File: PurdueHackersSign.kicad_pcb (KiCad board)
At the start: 2 copper layers, 73.7 x 134.6 mm, 43 parts, among them J1 Screw_Terminal_01x06, J2 Screw_Terminal_01x04, J3 Screw_Terminal_01x04, J4 Screw_Terminal_01x04, J5 Screw_Terminal_01x04, J6 Screw_Terminal_01x04, Q1 Q_NMOS_GDS, Q10 Q_NMOS_GDS, Q11 Q_NMOS_GDS, Q12 Q_NMOS_GDS, Q13 Q_NMOS_GDS, Q14 Q_NMOS_GDS, Q15 Q_NMOS_GDS, Q2 Q_NMOS_GDS, Q3 Q_NMOS_GDS, Q4 Q_NMOS_GDS, Q5 Q_NMOS_GDS, Q6 Q_NMOS_GDS, Q7 Q_NMOS_GDS, Q8 Q_NMOS_GDS, Q9 Q_NMOS_GDS, U1 RaspberryPi_Pico_W, U2 L7805, U3 25LCxxx

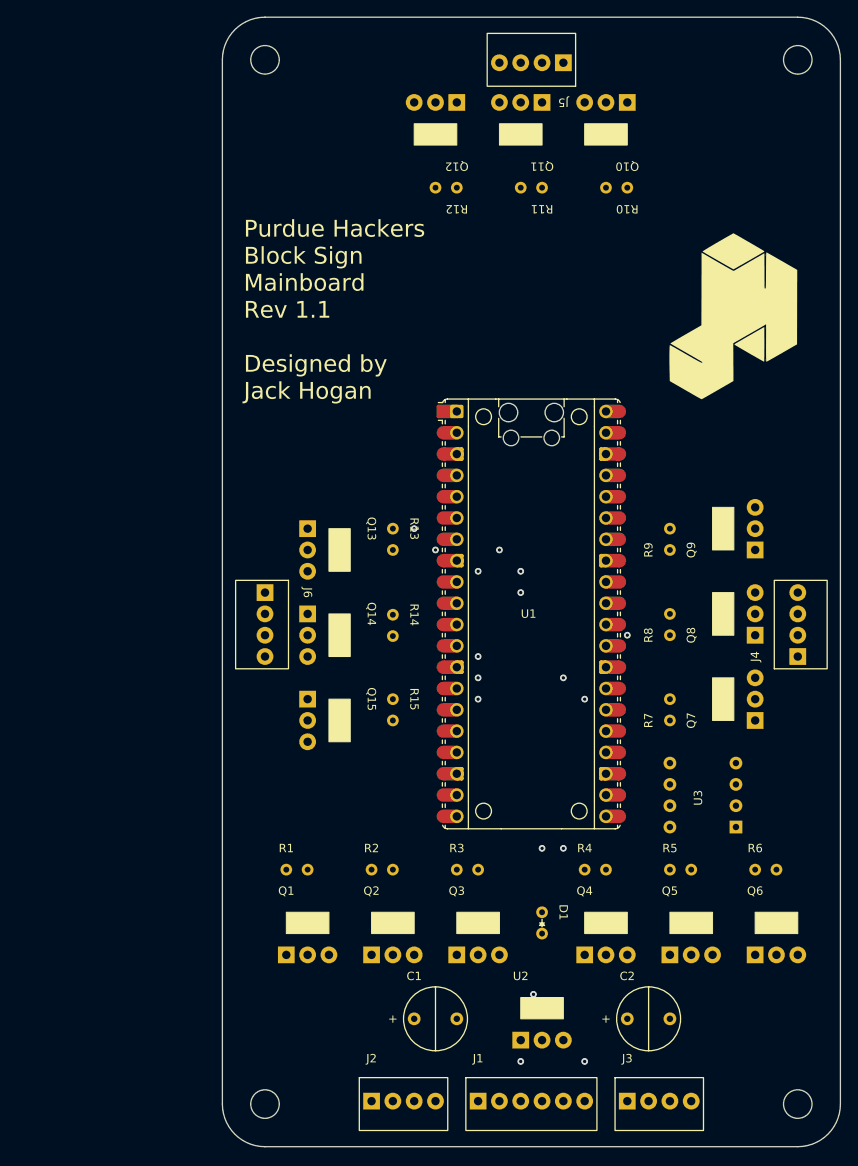
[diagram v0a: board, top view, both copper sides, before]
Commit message: Re-drew the schematic, re-assigned all the symbols, and re-routed the PCB
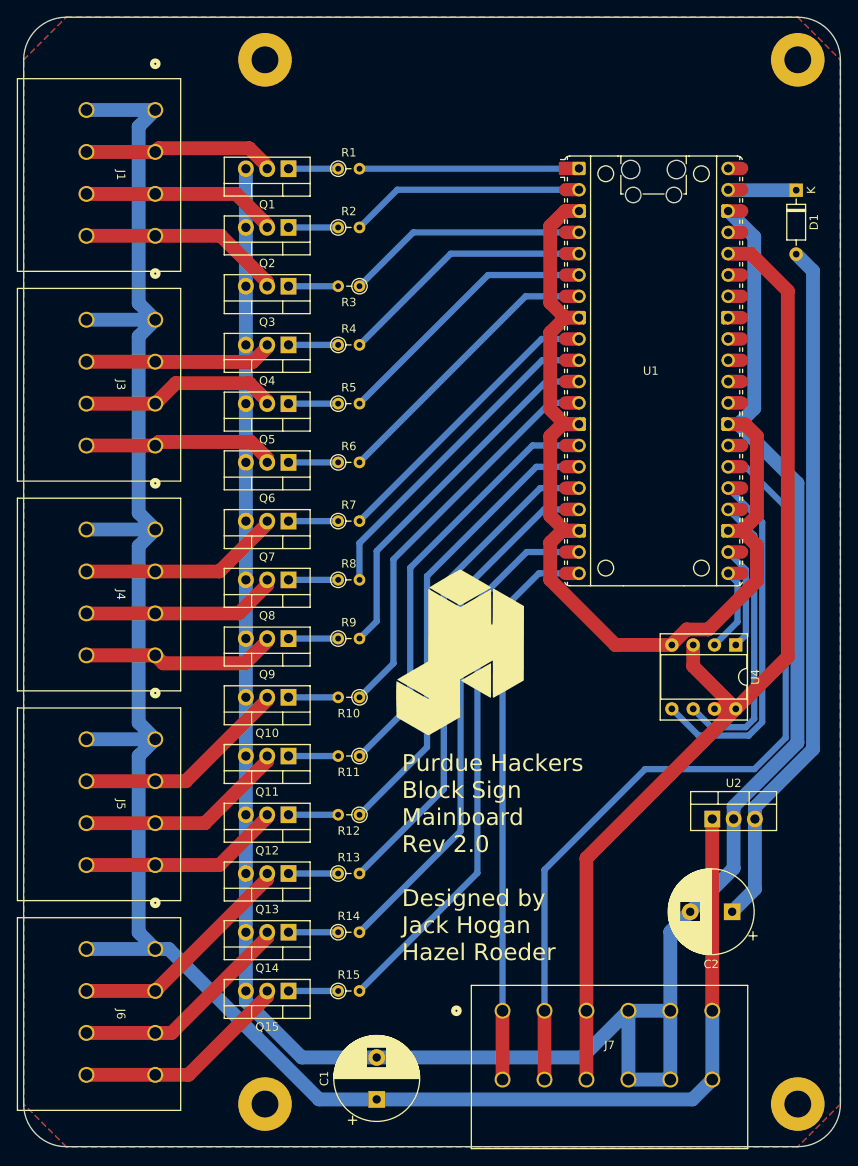
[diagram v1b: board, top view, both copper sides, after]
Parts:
- removed J2: Screw_Terminal_01x04, UsefulComponents:TerminalBlock_Adafruit-4
- removed U3: 25LCxxx, UsefulComponents:25LC1024
- added ?: , , F.Cu at (81.3, 33.0)
- added ?: , , F.Cu at (144.8, 157.5)
- added ?: , , F.Cu at (144.8, 33.0)
- added J7: 2604-1106, Local Footprints:CONN_2604-1106_WAG, F.Cu at (109.6, 146.4)
- added REF**: MountingHole_3.2mm_M3_Pad, MountingHole:MountingHole_3.2mm_M3_Pad, F.Cu at (81.3, 157.5)
- added U4: 25LCxxx, Package_DIP:DIP-8_W7.62mm_Socket, F.Cu at (137.4, 102.8)
- C1, C2: footprint UsefulComponents:PolarizedCapacitor -> Capacitor_THT:CP_Radial_D10.0mm_P5.00mm
- D1: footprint UsefulComponents:Diode -> Diode_THT:D_DO-35_SOD27_P7.62mm_Horizontal
- J1: value Screw_Terminal_01x06 -> 2604-1104; footprint UsefulComponents:TerminalBlock_Adafruit-6 -> Local Footprints:CONN_2604-1104_WAG
- J3, J4, J5, J6: value Screw_Terminal_01x04 -> 2604-1104; footprint UsefulComponents:TerminalBlock_Adafruit-4 -> Local Footprints:CONN_2604-1104_WAG
- Q1, Q10, Q11, Q12, Q13, Q14, Q15, Q2, Q3, Q4, Q5, Q6, Q7, Q8, Q9: footprint UsefulComponents:Adafruit_NMOS_GDS -> Package_TO_SOT_THT:TO-220-3_Vertical
- R1, R10, R11, R12, R13, R14, R15, R2, R3, R4, R5, R6, R7, R8, R9: footprint UsefulComponents:VerticalResistor -> Resistor_THT:R_Axial_DIN0204_L3.6mm_D1.6mm_P2.54mm_Vertical
- U2: footprint UsefulComponents:L7805 -> Package_TO_SOT_THT:TO-220-3_Vertical
- moved J1 124.2 mm to (68.2, 39.0), turned to -90 degrees
- moved J3 108.8 mm to (68.2, 64.0), turned to -90 degrees
- moved J5 94.2 mm to (68.2, 114.0), turned to -90 degrees
- moved Q1 93.7 mm to (84.1, 46.0), turned to 180 degrees
- moved D1 91.2 mm to (144.6, 48.6)
- moved Q2 87.3 mm to (84.1, 53.0), turned to 180 degrees
- moved Q12 87.2 mm to (84.1, 123.0)
- moved R1 83.8 mm to (90.0, 46.0)
- moved Q11 83.6 mm to (84.1, 116.0)
- moved Q3 82.2 mm to (84.1, 60.0), turned to 180 degrees
- moved Q10 81.6 mm to (84.1, 109.0)
- moved Q6 80.9 mm to (84.1, 81.0), turned to 180 degrees
- moved Q4 80.8 mm to (84.1, 67.0), turned to 180 degrees
- moved Q5 79.9 mm to (84.1, 74.0), turned to 180 degrees
- moved J4 78.1 mm to (68.2, 89.0), turned to -90 degrees
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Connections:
- net Net-(D1-K) renamed RP2040_VSYS
- net Net-(U1-GPIO0) renamed LED_CENTER_R_SIG
- net Net-(U1-GPIO1) renamed LED_CENTER_G_SIG
- net Net-(U1-GPIO10) renamed LED_RIGHT_G_SIG
- net Net-(U1-GPIO11) renamed LED_RIGHT_B_SIG
- net Net-(U1-GPIO12) renamed LED_TOP_R_SIG
- net Net-(U1-GPIO13) renamed LED_TOP_G_SIG
- net Net-(U1-GPIO14) renamed LED_TOP_B_SIG
- net Net-(U1-GPIO3) renamed LED_BOTTOM_LEFT_R_SIG
- net Net-(U1-GPIO4) renamed LED_BOTTOM_LEFT_G_SIG
- net Net-(U1-GPIO5) renamed LED_BOTTOM_LEFT_B_SIG
- net Net-(U1-GPIO6) renamed LED_BOTTOM_RIGHT_R_SIG
- net Net-(U1-GPIO7) renamed LED_BOTTOM_RIGHT_G_SIG
- net Net-(U1-GPIO8) renamed LED_BOTTOM_RIGHT_B_SIG
- net Net-(U1-GPIO9) renamed LED_RIGHT_R_SIG
- Q1 pad 2: Net-(J2-Pin_2) -> LED_CENTER_B_GND
- Q10 pad 2: Net-(J5-Pin_2) -> LED_RIGHT_B_GND
- Q11 pad 2: Net-(J5-Pin_3) -> LED_RIGHT_R_GND
- Q12 pad 2: Net-(J5-Pin_4) -> LED_RIGHT_G_GND
- Q13 pad 2: Net-(J6-Pin_2) -> LED_TOP_B_GND
- Q14 pad 2: Net-(J6-Pin_3) -> LED_TOP_R_GND
- Q15 pad 2: Net-(J6-Pin_4) -> LED_TOP_G_GND
- Q2 pad 2: Net-(J2-Pin_3) -> LED_CENTER_R_GND
- Q3 pad 2: Net-(J2-Pin_4) -> LED_CENTER_G_GND
- Q4 pad 2: Net-(J3-Pin_2) -> LED_BOTTOM_LEFT_B_GND
- Q5 pad 2: Net-(J3-Pin_3) -> LED_BOTTOM_LEFT_R_GND
- Q6 pad 2: Net-(J3-Pin_4) -> LED_BOTTOM_LEFT_G_GND
- Q7 pad 2: Net-(J4-Pin_2) -> LED_BOTTOM_RIGHT_B_GND
- Q8 pad 2: Net-(J4-Pin_3) -> LED_BOTTOM_RIGHT_R_GND
- Q9 pad 2: Net-(J4-Pin_4) -> LED_BOTTOM_RIGHT_G_GND
- R3 pad 1: Net-(Q3-G) -> LED_CENTER_B_SIG
- R3 pad 2: Net-(U1-GPIO2) -> Net-(Q3-G)
- U1 pad 20: Button Contact -> BUTTON_SWITCH
- U1 pad 21: Net-(U1-GPIO16) -> EEPROM_MISO
- U1 pad 22: Net-(U1-GPIO17) -> EEPROM_CS
- U1 pad 24: Net-(U1-GPIO18) -> EEPROM_SCK
- U1 pad 25: Net-(U1-GPIO19) -> EEPROM_MOSI
- U1 pad 26: Button LED -> BUTTON_LED
- U1 pad 36: Net-(J1-Pin_4) -> +3.3V
- U1 pad 4: Net-(U1-GPIO2) -> LED_CENTER_B_SIG
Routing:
- net GND: track 0.00 -> 399.0 mm, vias 4 -> 0
- net +12V: track 0.00 -> 253.4 mm
- net +3.3V: track 0.00 -> 126.2 mm
- net BUTTON_LED: track 0.00 -> 96.6 mm
- net Net-(D1-A): track 0.00 -> 83.2 mm
- net BUTTON_SWITCH: track 0.00 -> 66.9 mm
- net LED_TOP_B_SIG: track 0.00 -> 66.8 mm
- net LED_TOP_G_SIG: track 0.00 -> 63.7 mm
- net LED_TOP_R_SIG: track 0.00 -> 59.5 mm
- net LED_RIGHT_B_SIG: track 0.00 -> 55.3 mm
- net LED_RIGHT_G_SIG: track 0.00 -> 51.1 mm
- net LED_RIGHT_R_SIG: track 0.00 -> 48.0 mm
- net LED_BOTTOM_RIGHT_B_SIG: track 0.00 -> 43.8 mm, vias 1 -> 0
- net EEPROM_MOSI: track 0.00 -> 42.3 mm
- net LED_BOTTOM_RIGHT_G_SIG: track 0.00 -> 39.6 mm, vias 1 -> 0
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- added copper zone on B.Cu, net GND
- added copper zone on F.Cu, net GND
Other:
- board size 73.7 x 134.6 mm -> 97.3 x 134.6 mm
- board text added: "Purdue Hackers Block Sign Mainboard Rev 2.0 Designed by Jack Hogan Hazel Roeder"
- board text removed: "Purdue Hackers Block Sign Mainboard Rev 1.1 Designed by Jack Hogan"

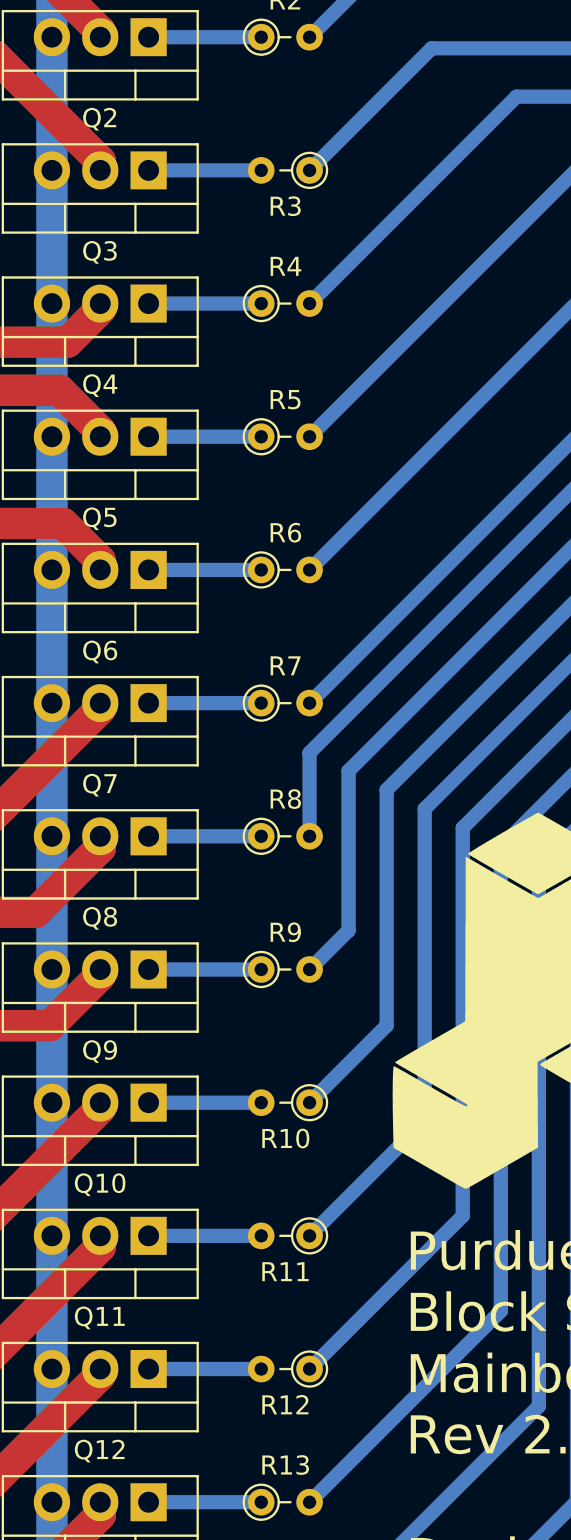
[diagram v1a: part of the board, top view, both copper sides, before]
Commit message: Modified some silkscreen properties for fabrication
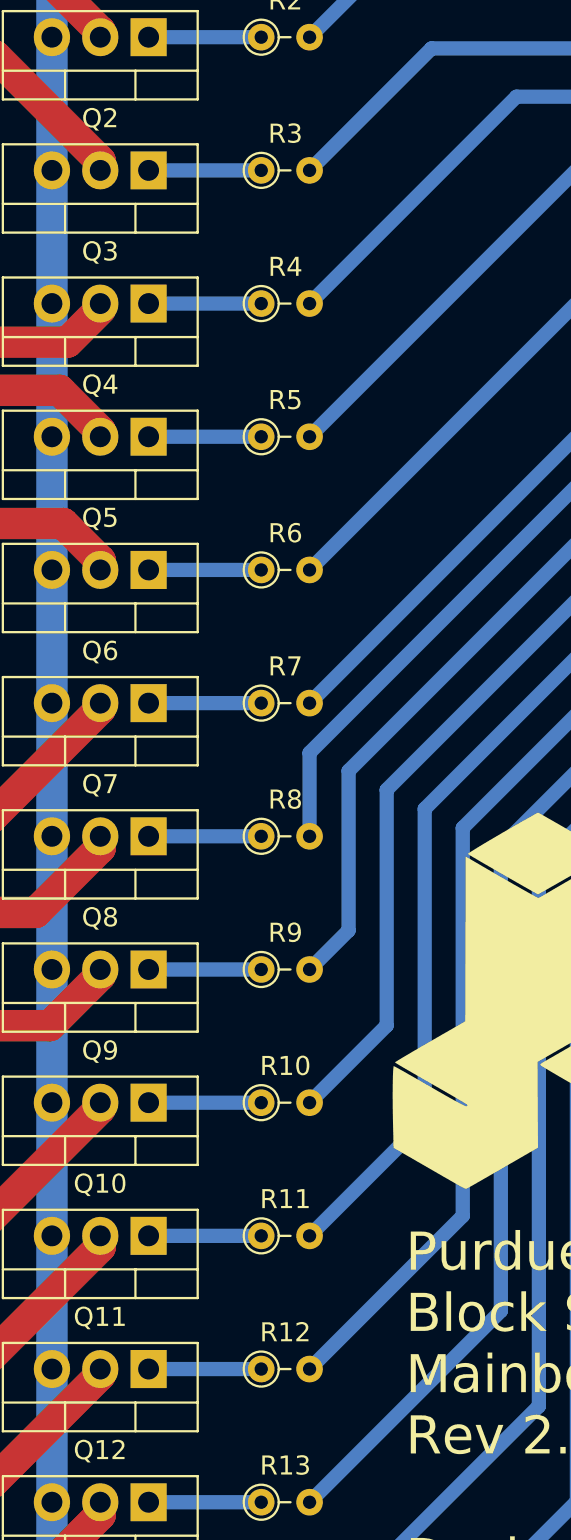
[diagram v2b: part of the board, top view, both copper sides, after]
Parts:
- moved R10 2.54 mm to (90.0, 109.0), turned to 0 degrees
- moved R11 2.54 mm to (90.0, 116.0), turned to 0 degrees
- moved R12 2.54 mm to (90.0, 123.0), turned to 0 degrees
- moved R3 2.54 mm to (90.0, 60.0), turned to 0 degrees
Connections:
- R10 pad 1: LED_RIGHT_R_SIG -> Net-(Q10-G)
- R10 pad 2: Net-(Q10-G) -> LED_RIGHT_R_SIG
- R11 pad 1: LED_RIGHT_G_SIG -> Net-(Q11-G)
- R11 pad 2: Net-(Q11-G) -> LED_RIGHT_G_SIG
- R12 pad 1: LED_RIGHT_B_SIG -> Net-(Q12-G)
- R12 pad 2: Net-(Q12-G) -> LED_RIGHT_B_SIG
- R3 pad 1: LED_CENTER_B_SIG -> Net-(Q3-G)
- R3 pad 2: Net-(Q3-G) -> LED_CENTER_B_SIG
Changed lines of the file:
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@@
   (setup
     (pad_to_mask_clearance 0)
-    (grid_origin 144.780001 157.480002)
+    (grid_origin 54 29.427896)
     (pcbplotparams
       (layerselection 0x00010fc_ffffffff)
@@
       (drillshape 0)
       (scaleselection 1)
-      (outputdirectory "fab/")
+      (outputdirectory "../phsign-fab/")
     )
   )
@@
   )
   (footprint "Resistor_THT:R_Axial_DIN0204_L3.6mm_D1.6mm_P2.54mm_Vertical" (layer "F.Cu")
-    (at 92.54 60.000001 180)
+    (at 90 60.000001)
     (descr "Resistor, Axial_DIN0204 series, Axial, Vertical, pin pitch=2.54mm, 0.167W, length*diameter=3.6*1.6mm^2, http://cdn-reichelt.de/documents/datenblatt/B400/1_4W%23YAG.pdf")
     (tags "Resistor Axial_DIN0204 series Axial Vertical pin pitch 2.54mm 0.167W length 3.6mm diameter 1.6mm")
@@
     (fp_circle (center 0 0) (end 0.8 0)
       (stroke (width 0.1) (type solid)) (fill none) (layer "F.Fab"))
-    (pad "1" thru_hole circle (at 0 0 180) (size 1.4 1.4) (drill 0.7) (layers "*.Cu" "*.Mask")
-      (net 49 "LED_CENTER_B_SIG") (pintype "passive"))
-    (pad "2" thru_hole oval (at 2.54 0 180) (size 1.4 1.4) (drill 0.7) (layers "*.Cu" "*.Mask")
+    (pad "1" thru_hole circle (at 0 0) (size 1.4 1.4) (drill 0.7) (layers "*.Cu" "*.Mask")
       (net 11 "Net-(Q3-G)") (pintype "passive"))
+    (pad "2" thru_hole oval (at 2.54 0) (size 1.4 1.4) (drill 0.7) (layers "*.Cu" "*.Mask")
+      (net 49 "LED_CENTER_B_SIG") (pintype "passive"))
     (model "${KICAD6_3DMODEL_DIR}/Resistor_THT.3dshapes/R_Axial_DIN0204_L3.6mm_D1.6mm_P2.54mm_Vertical.wrl"
       (offset (xyz 0 0 0))
@@
   )
   (footprint "Resistor_THT:R_Axial_DIN0204_L3.6mm_D1.6mm_P2.54mm_Vertical" (layer "F.Cu")
-    (at 92.54 116.000001 180)
+    (at 90 116.000001)
     (descr "Resistor, Axial_DIN0204 series, Axial, Vertical, pin pitch=2.54mm, 0.167W, length*diameter=3.6*1.6mm^2, http://cdn-reichelt.de/documents/datenblatt/B400/1_4W%23YAG.pdf")
     (tags "Resistor Axial_DIN0204 series Axial Vertical pin pitch 2.54mm 0.167W length 3.6mm diameter 1.6mm")
@@
     (fp_circle (center 0 0) (end 0.8 0)
       (stroke (width 0.1) (type solid)) (fill none) (layer "F.Fab"))
-    (pad "1" thru_hole circle (at 0 0 180) (size 1.4 1.4) (drill 0.7) (layers "*.Cu" "*.Mask")
-      (net 57 "LED_RIGHT_G_SIG") (pintype "passive"))
-    (pad "2" thru_hole oval (at 2.54 0 180) (size 1.4 1.4) (drill 0.7) (layers "*.Cu" "*.Mask")
+    (pad "1" thru_hole circle (at 0 0) (size 1.4 1.4) (drill 0.7) (layers "*.Cu" "*.Mask")
       (net 19 "Net-(Q11-G)") (pintype "passive"))
+    (pad "2" thru_hole oval (at 2.54 0) (size 1.4 1.4) (drill 0.7) (layers "*.Cu" "*.Mask")
+      (net 57 "LED_RIGHT_G_SIG") (pintype "passive"))
     (model "${KICAD6_3DMODEL_DIR}/Resistor_THT.3dshapes/R_Axial_DIN0204_L3.6mm_D1.6mm_P2.54mm_Vertical.wrl"
       (offset (xyz 0 0 0))
@@
   )
   (footprint "Resistor_THT:R_Axial_DIN0204_L3.6mm_D1.6mm_P2.54mm_Vertical" (layer "F.Cu")
-    (at 92.54 123.000001 180)
+    (at 90 123.000001)
     (descr "Resistor, Axial_DIN0204 series, Axial, Vertical, pin pitch=2.54mm, 0.167W, length*diameter=3.6*1.6mm^2, http://cdn-reichelt.de/documents/datenblatt/B400/1_4W%23YAG.pdf")
     (tags "Resistor Axial_DIN0204 series Axial Vertical pin pitch 2.54mm 0.167W length 3.6mm diameter 1.6mm")
@@
     (fp_circle (center 0 0) (end 0.8 0)
       (stroke (width 0.1) (type solid)) (fill none) (layer "F.Fab"))
-    (pad "1" thru_hole circle (at 0 0 180) (size 1.4 1.4) (drill 0.7) (layers "*.Cu" "*.Mask")
-      (net 58 "LED_RIGHT_B_SIG") (pintype "passive"))
-    (pad "2" thru_hole oval (at 2.54 0 180) (size 1.4 1.4) (drill 0.7) (layers "*.Cu" "*.Mask")
+    (pad "1" thru_hole circle (at 0 0) (size 1.4 1.4) (drill 0.7) (layers "*.Cu" "*.Mask")
       (net 20 "Net-(Q12-G)") (pintype "passive"))
+    (pad "2" thru_hole oval (at 2.54 0) (size 1.4 1.4) (drill 0.7) (layers "*.Cu" "*.Mask")
+      (net 58 "LED_RIGHT_B_SIG") (pintype "passive"))
     (model "${KICAD6_3DMODEL_DIR}/Resistor_THT.3dshapes/R_Axial_DIN0204_L3.6mm_D1.6mm_P2.54mm_Vertical.wrl"
       (offset (xyz 0 0 0))
@@
   )
   (footprint "Resistor_THT:R_Axial_DIN0204_L3.6mm_D1.6mm_P2.54mm_Vertical" (layer "F.Cu")
-    (at 92.54 109.000001 180)
+    (at 90 109.000001)
     (descr "Resistor, Axial_DIN0204 series, Axial, Vertical, pin pitch=2.54mm, 0.167W, length*diameter=3.6*1.6mm^2, http://cdn-reichelt.de/documents/datenblatt/B400/1_4W%23YAG.pdf")
     (tags "Resistor Axial_DIN0204 series Axial Vertical pin pitch 2.54mm 0.167W length 3.6mm diameter 1.6mm")
@@
     (fp_circle (center 0 0) (end 0.8 0)
       (stroke (width 0.1) (type solid)) (fill none) (layer "F.Fab"))
-    (pad "1" thru_hole circle (at 0 0 180) (size 1.4 1.4) (drill 0.7) (layers "*.Cu" "*.Mask")
-      (net 56 "LED_RIGHT_R_SIG") (pintype "passive"))
-    (pad "2" thru_hole oval (at 2.54 0 180) (size 1.4 1.4) (drill 0.7) (layers "*.Cu" "*.Mask")
+    (pad "1" thru_hole circle (at 0 0) (size 1.4 1.4) (drill 0.7) (layers "*.Cu" "*.Mask")
       (net 18 "Net-(Q10-G)") (pintype "passive"))
+    (pad "2" thru_hole oval (at 2.54 0) (size 1.4 1.4) (drill 0.7) (layers "*.Cu" "*.Mask")
+      (net 56 "LED_RIGHT_R_SIG") (pintype "passive"))
     (model "${KICAD6_3DMODEL_DIR}/Resistor_THT.3dshapes/R_Axial_DIN0204_L3.6mm_D1.6mm_P2.54mm_Vertical.wrl"
       (offset (xyz 0 0 0))

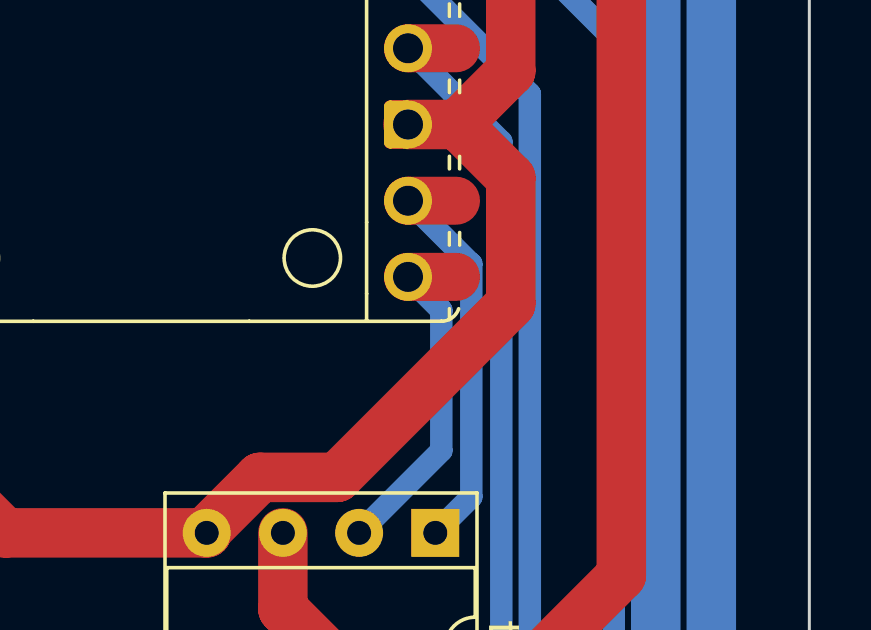
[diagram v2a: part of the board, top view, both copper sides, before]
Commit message: Switched button LED and switch lines
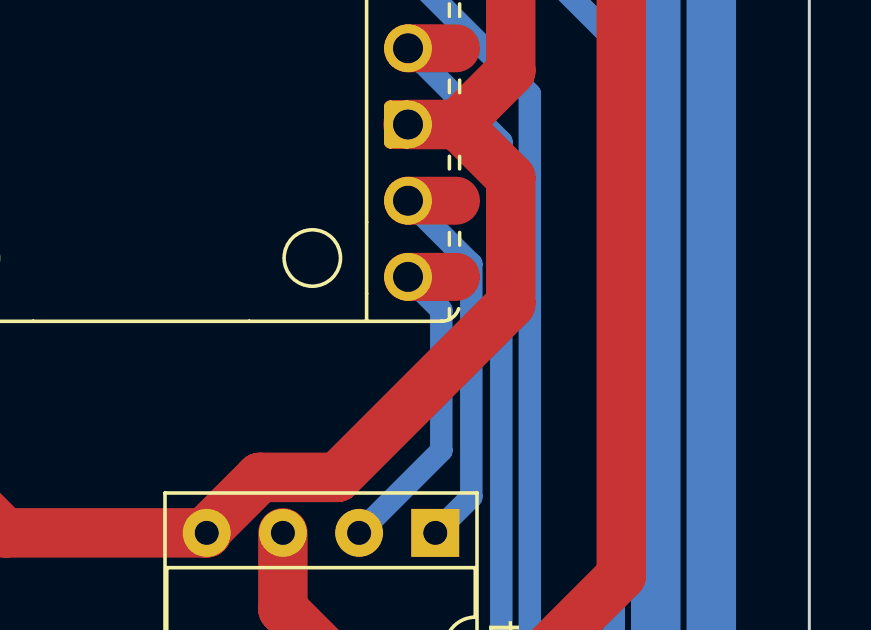
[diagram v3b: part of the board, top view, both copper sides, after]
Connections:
- J7 pad 1_1: BUTTON_SWITCH -> BUTTON_LED
- J7 pad 1_2: BUTTON_SWITCH -> BUTTON_LED
- J7 pad 2_1: BUTTON_LED -> BUTTON_SWITCH
- J7 pad 2_2: BUTTON_LED -> BUTTON_SWITCH
- U1 pad 20: BUTTON_SWITCH -> BUTTON_LED
- U1 pad 26: BUTTON_LED -> BUTTON_SWITCH
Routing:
- net BUTTON_SWITCH: track 66.9 -> 96.6 mm
- net BUTTON_LED: track 96.6 -> 66.9 mm
